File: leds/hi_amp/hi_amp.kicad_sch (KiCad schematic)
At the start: 20 parts

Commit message: WIP hi_amp leds
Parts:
- removed H1, H2, H3, H4: MountingHole_Pad, MountingHole:MountingHole_4mm_Pad_Via, symbol Mechanical:MountingHole_Pad
- added CN1, CN2, CN3: 428192213, easyeda2kicad:CONN-TH_0428192214, symbol easyeda2kicad:428192213
- renumbered H5 to H1, H6 to H2, H7 to H3, H8 to H4, TP5 to TP1, TP11 to TP10, TP16 to TP11, TP6 to TP2, TP7 to TP3, TP8 to TP4, TP13 to TP5, TP9 to TP6, TP14 to TP7, TP10 to TP8, TP15 to TP9
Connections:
- net GND: now also CN1.1, CN1.3, CN2.1, CN2.3, CN3.1, CN3.3
- net buckconverter/VIN: now also CN1.2, CN1.4, CN2.2, CN2.4, CN3.2, CN3.4
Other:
- removed sheet usbcpd

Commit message: WIP: add vias to buck (after fabrication).
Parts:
- added TP101: LabeledTestPoint, easyeda2kicad:LabeledTestPoint, symbol easyeda2kicad:LabeledTestPoint
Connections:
- net buckconverter/VIN renamed VSYS
- net VSYS: now also TP101.1
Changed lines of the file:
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@@
 		(color 0 0 0 0)
 	)
+	(junction
+		(at 49.53 36.83)
+		(diameter 0)
+		(color 0 0 0 0)
+	)
 	(wire
 		(pts
@@
 	(wire
 		(pts
-			(xy 49.53 36.83) (xy 45.72 36.83)
+			(xy 45.72 36.83) (xy 49.53 36.83)
 		)
 		(stroke
@@
 		(pts
 			(xy 125.73 24.13) (xy 114.3 24.13)
+		)
+		(stroke
+			(width 0)
+			(type default)
+		)
+	)
+	(wire
+		(pts
+			(xy 49.53 36.83) (xy 60.96 36.83)
 		)
 		(stroke
@@
 	(label "5V"
 		(at 88.9 20.32 0)
+		(effects
+			(font
+				(size 1.27 1.27)
+			)
+			(justify left bottom)
+		)
+	)
+	(label "VSYS"
+		(at 36.83 36.83 0)
 		(effects
 			(font
@@
 	)
 	(symbol
+		(lib_id "easyeda2kicad:LabeledTestPoint")
+		(at 49.53 36.83 0)
+		(unit 1)
+		(exclude_from_sim no)
+		(in_bom no)
+		(on_board yes)
+		(dnp no)
+		(fields_autoplaced yes)
+		(property "Reference" "TP101"
+			(at 49.53 29.972 0)
+			(effects
+				(font
+					(size 1.27 1.27)
+				)
+				(hide yes)
+			)
+		)
+		(property "Value" "LabeledTestPoint"
+			(at 49.53 31.75 0)
+			(effects
+				(font
+					(size 1.27 1.27)
+				)
+				(hide yes)
+			)
+		)
+		(property "Footprint" "easyeda2kicad:LabeledTestPoint"
+			(at 54.61 36.83 0)
+			(effects
+				(font
+					(size 1.27 1.27)
+				)
+				(hide yes)
+			)
+		)
+		(property "Datasheet" "~"
+			(at 54.61 36.83 0)
+			(effects
+				(font
+					(size 1.27 1.27)
+				)
+				(hide yes)
+			)
+		)
+		(property "Description" "test point"
+			(at 49.53 36.83 0)
+			(effects
+				(font
+					(size 1.27 1.27)
+				)
+				(hide yes)
+			)
+		)
+		(property "Label" "VSYS"
+			(at 52.07 33.5279 0)
+			(effects
+				(font
+					(size 1.27 1.27)
+				)
+				(justify left)
+			)
+		)
+		(pin "1"
+		)
+		(instances
+			(project ""
+				(path "/48ddfdd8-68fa-4e63-aa18-bc113cdf8cfa"
+					(reference "TP101")
+					(unit 1)
+				)
+			)
+		)
+	)
+	(symbol
 		(lib_id "easyeda2kicad:428192213")
 		(at 27.94 39.37 180)
@@
 	)
 	(sheet
-		(at 49.53 24.13)
-		(size 26.67 25.4)
+		(at 60.96 31.75)
+		(size 15.24 10.16)
 		(exclude_from_sim no)
 		(in_bom yes)
@@
 		)
 		(property "Sheetname" "buckconverter"
-			(at 49.53 23.4184 0)
+			(at 60.96 31.0384 0)
 			(effects
 				(font
@@
 		)
 		(property "Sheetfile" "buckconverter.kicad_sch"
-			(at 49.53 49.4796 0)
+			(at 60.96 42.4946 0)
 			(effects
 				(font
@@
 		)
 		(pin "VIN" input
-			(at 49.53 36.83 180)
-			(effects
-				(font
+			(at 60.96 36.83 180)
+			(effects
+				(font

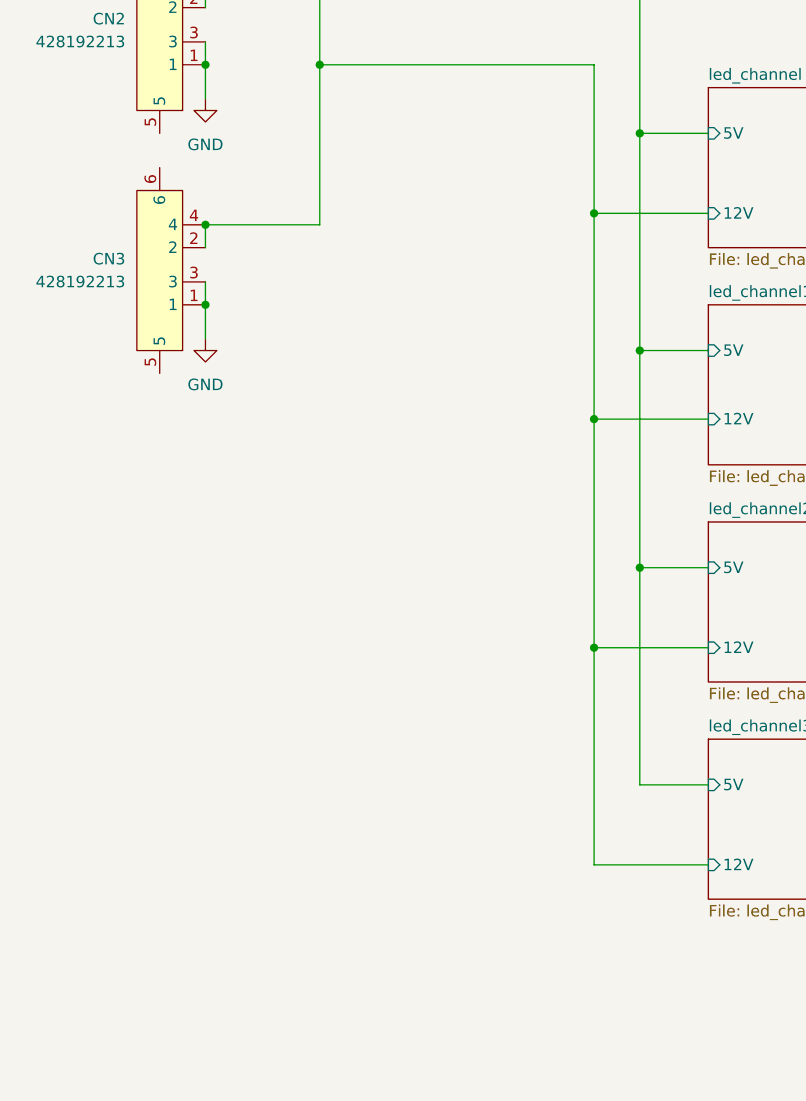
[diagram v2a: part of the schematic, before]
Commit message: add stronger gate driver to LEDs
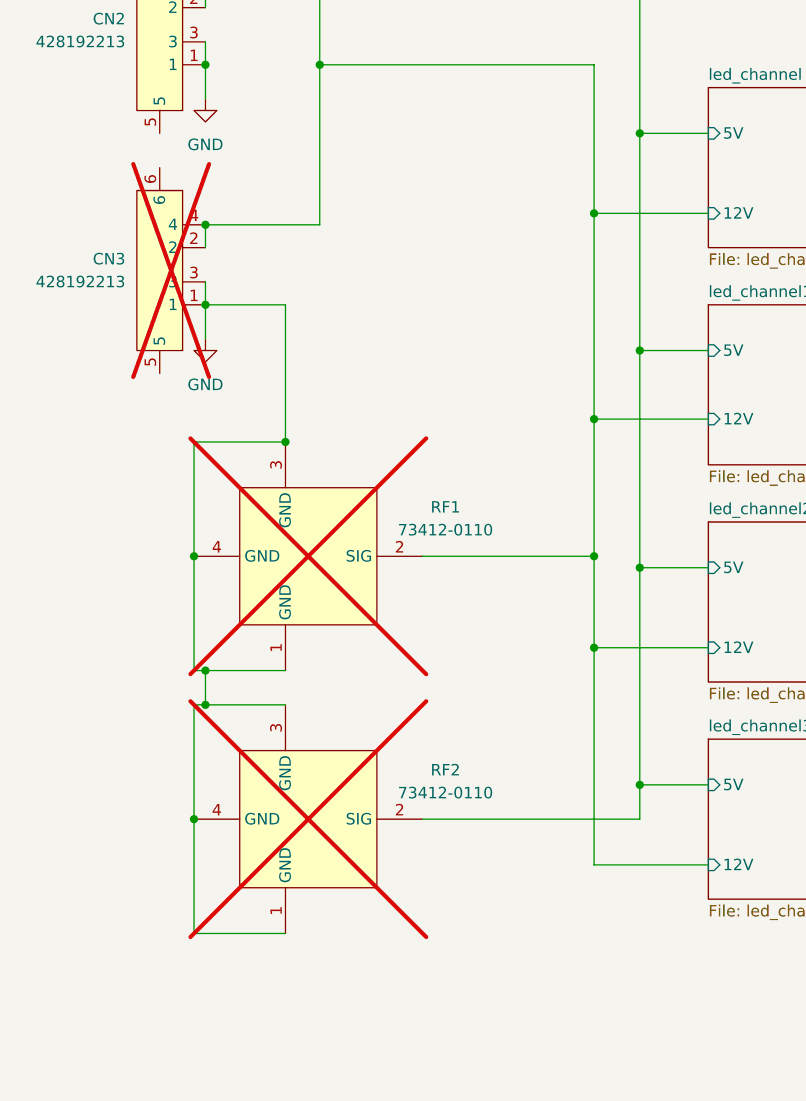
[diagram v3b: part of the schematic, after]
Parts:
- added RF1, RF2: 73412-0110, easyeda2kicad:ANT-SMD_73412-0110, symbol easyeda2kicad:73412-0110
- CN3: now not fitted; now left out of the parts list
- renumbered TP101 to TP1, TP9 to TP10, TP10 to TP11, TP11 to TP12, TP12 to TP13, TP1 to TP2, TP2 to TP3, TP3 to TP4, TP4 to TP5, TP5 to TP6, TP6 to TP7, TP7 to TP8, TP8 to TP9
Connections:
- net 5V: now also RF2.2 (SIG)
- net GND: now also RF1.1 (GND), RF1.3 (GND), RF1.4 (GND), RF2.1 (GND), RF2.3 (GND), RF2.4 (GND)
- net VSYS: now also RF1.2 (SIG)
